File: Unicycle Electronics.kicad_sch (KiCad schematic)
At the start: 0 parts

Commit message: Initial mock
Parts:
- added D1, D?: BXRE-30G20F0-C-83, symbol Device:LED
- added D2: Rear_LED_12V, symbol Device:LED
- added U1: LDH-65-700, symbol LED_Driver:LDH-65-700
- added U?: Stepdown_12V, symbol Converter_DCDC:DC_DC_Buck
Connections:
- new net: D2.2 (K), U1.1 (Vin+), U?.3 (Vout+)
- new net: D1.2 (K), D?.1 (A)
- new net: D?.2 (K), U1.3 (Vout+)
- new net: D1.1 (A), U1.4 (Vout-)
- new net DC_Source: D2.1 (A), U1.2 (Vin-), U?.1 (Vin+), U?.2 (Vin-), U?.4 (Vout-)

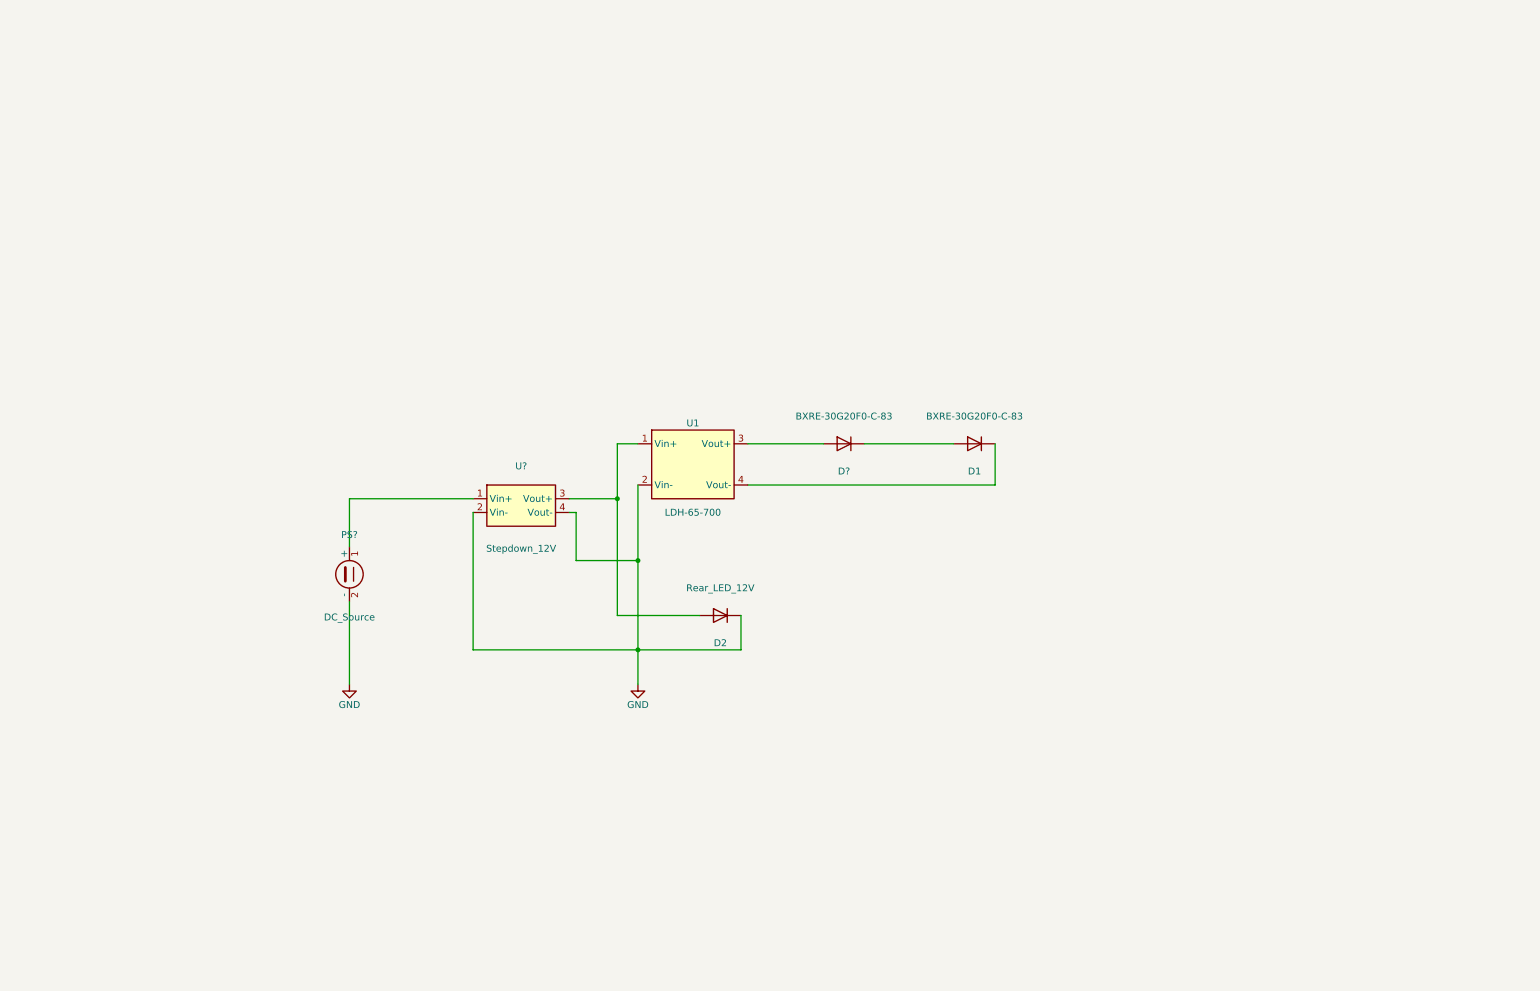
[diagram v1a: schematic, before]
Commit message: Schematic updates
Cleaned it up, added nets

TODO:
Change Diodes to some sort of connector, the LEDs are not on the PCB, they need to be plugged in

3.3v regulator for ESP32

BOOT and EN buttons for ESP32

Add PWM Dimming pins to LED driver

Switch 12v regulator to input on the PCB, meaning use a connector instead of the actual regulator. The regulator does not sit on the PCB
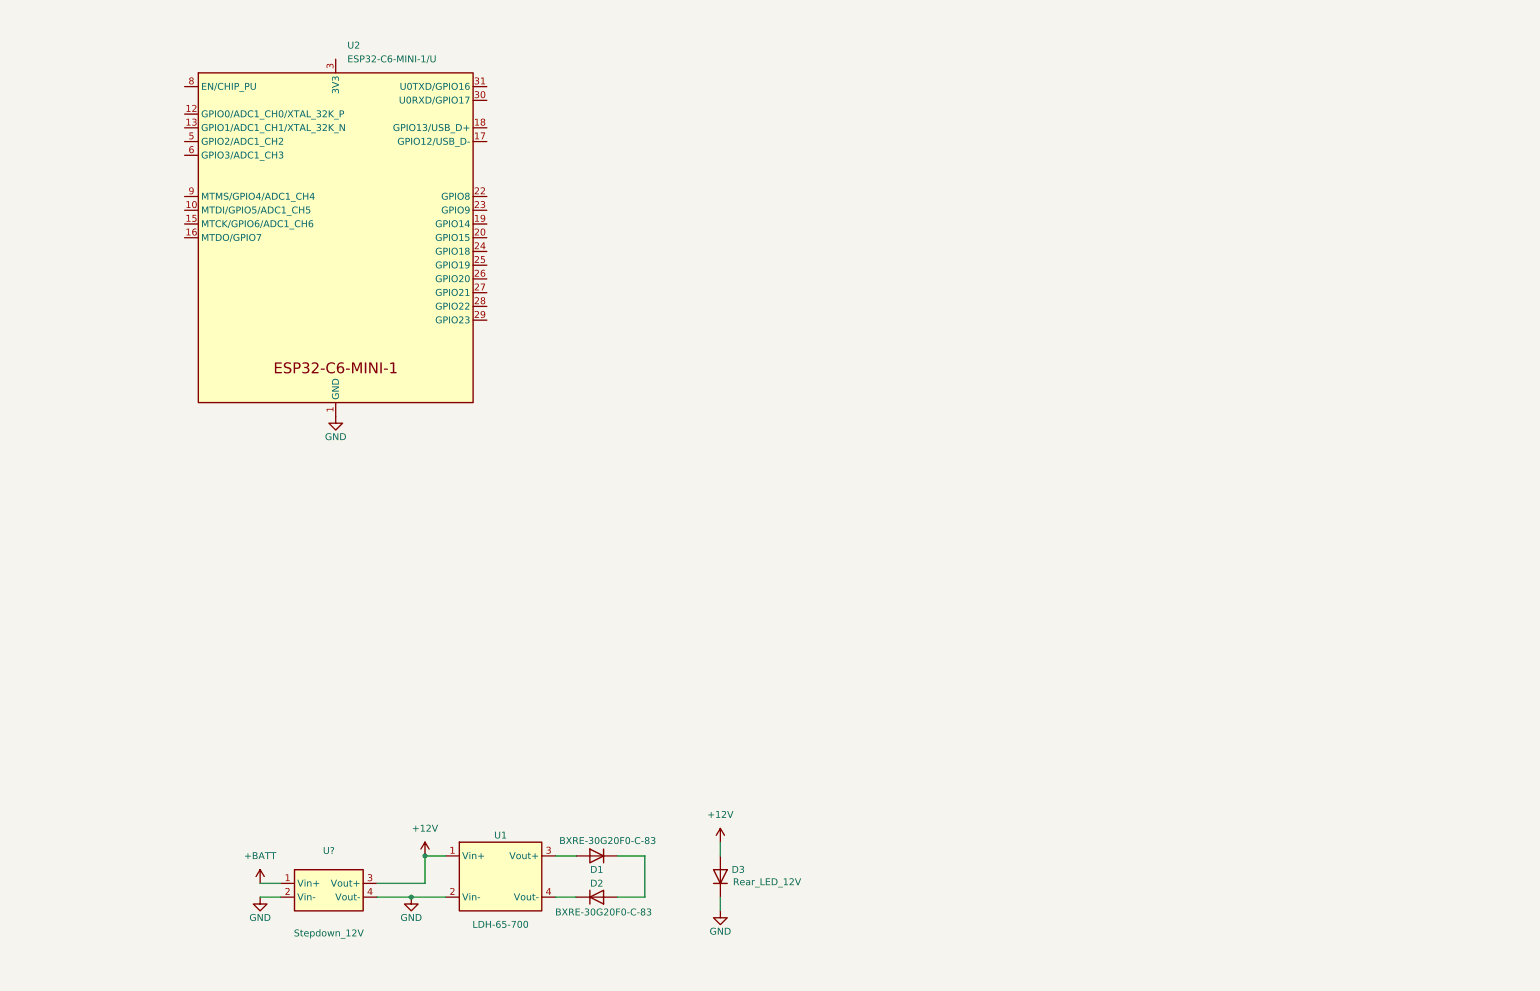
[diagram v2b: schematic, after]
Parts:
- added U2: ESP32-C6-MINI-1/U, PCM_Espressif:ESP32-C6-MINI-1, symbol PCM_Espressif:ESP32-C6-MINI-1/U
- gave numbers to parts that had none: 1
- renumbered D2 to D3
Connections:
- net +12V: now reaches D3.2 (K), U1.1 (Vin+), U?.3 (Vout+)
- net DC_Source renamed GND
- net GND: now also U2.1 (GND), U2.11 (GND), U2.14 (GND), U2.2 (GND), U2.36 (GND), U2.37 (GND), U2.38 (GND), U2.39 (GND), U2.40 (GND), U2.41 (GND), U2.42 (GND), U2.43 (GND), U2.44 (GND), U2.45 (GND), U2.46 (GND), U2.47 (GND), U2.48 (GND), U2.49 (GND), U2.50 (GND), U2.51 (GND), U2.52 (GND), U2.53 (GND); no longer U?.1 (Vin+)
- new net +BATT: U?.1 (Vin+)
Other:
- moved on the sheet: D1, D2, D3, U1, U?

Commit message: schematic update
This is what I have so far—let me know if you need any changes or want me to add anything.
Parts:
- added C1: 10uF, symbol Device:C
- added C2: 22uF, symbol Device:C
- added C3: 100nF, symbol Device:C
- added Q1: 2N7002, Package_TO_SOT_SMD:SOT-23, symbol Transistor_FET:2N7002
- added R1, R2, R4: 10k, symbol Device:R
- added R3: 1k, symbol Device:R
- added SW1: BOOT, symbol Switch:SW_Push
- added SW2: EN/Reset, symbol Switch:SW_Push
- added U3: AMS1117-3.3, Package_TO_SOT_SMD:SOT-223-3_TabPin2, symbol Regulator_Linear:AMS1117-3.3
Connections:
- net +12V: now also C1.1, U3.3 (VI)
- net GND: now also C1.2, C2.2, Q1.1 (S), R4.2, SW1.2, SW2.2, U3.1 (GND)
- net at U2.23 (GPIO9): now also R2.2, SW1.1
- net at U2.8 (EN/CHIP_PU): now also C3.1, R1.2
- new net: C3.2, SW2.1
- new net: Q1.2 (G), R3.2, R4.1
- new net +3.3V: C2.1, R1.1, R2.1, U3.2 (VO)
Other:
- note added: "3.3V Voltage Regulator"
- note added: "BOOT Button (GPIO9)"
- note added: "EN/Reset Button"
- note added: "PWM Dimming Control (GPIO2)"
- moved on the sheet: U2

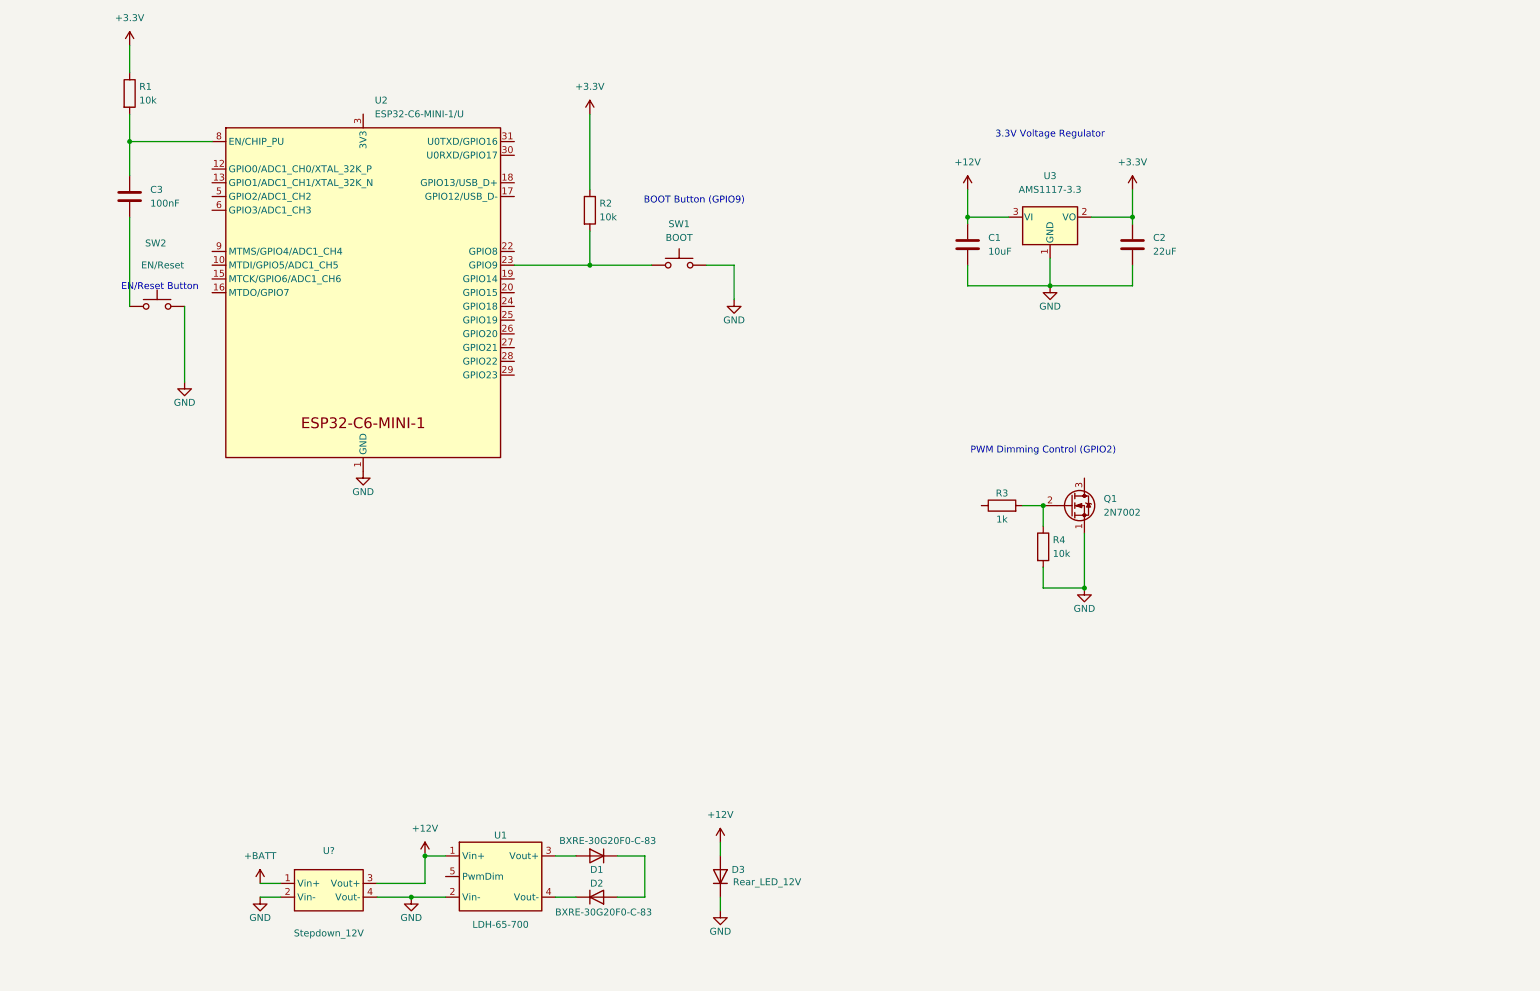
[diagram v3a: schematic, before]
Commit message: Updated TODO list, Changed EN button
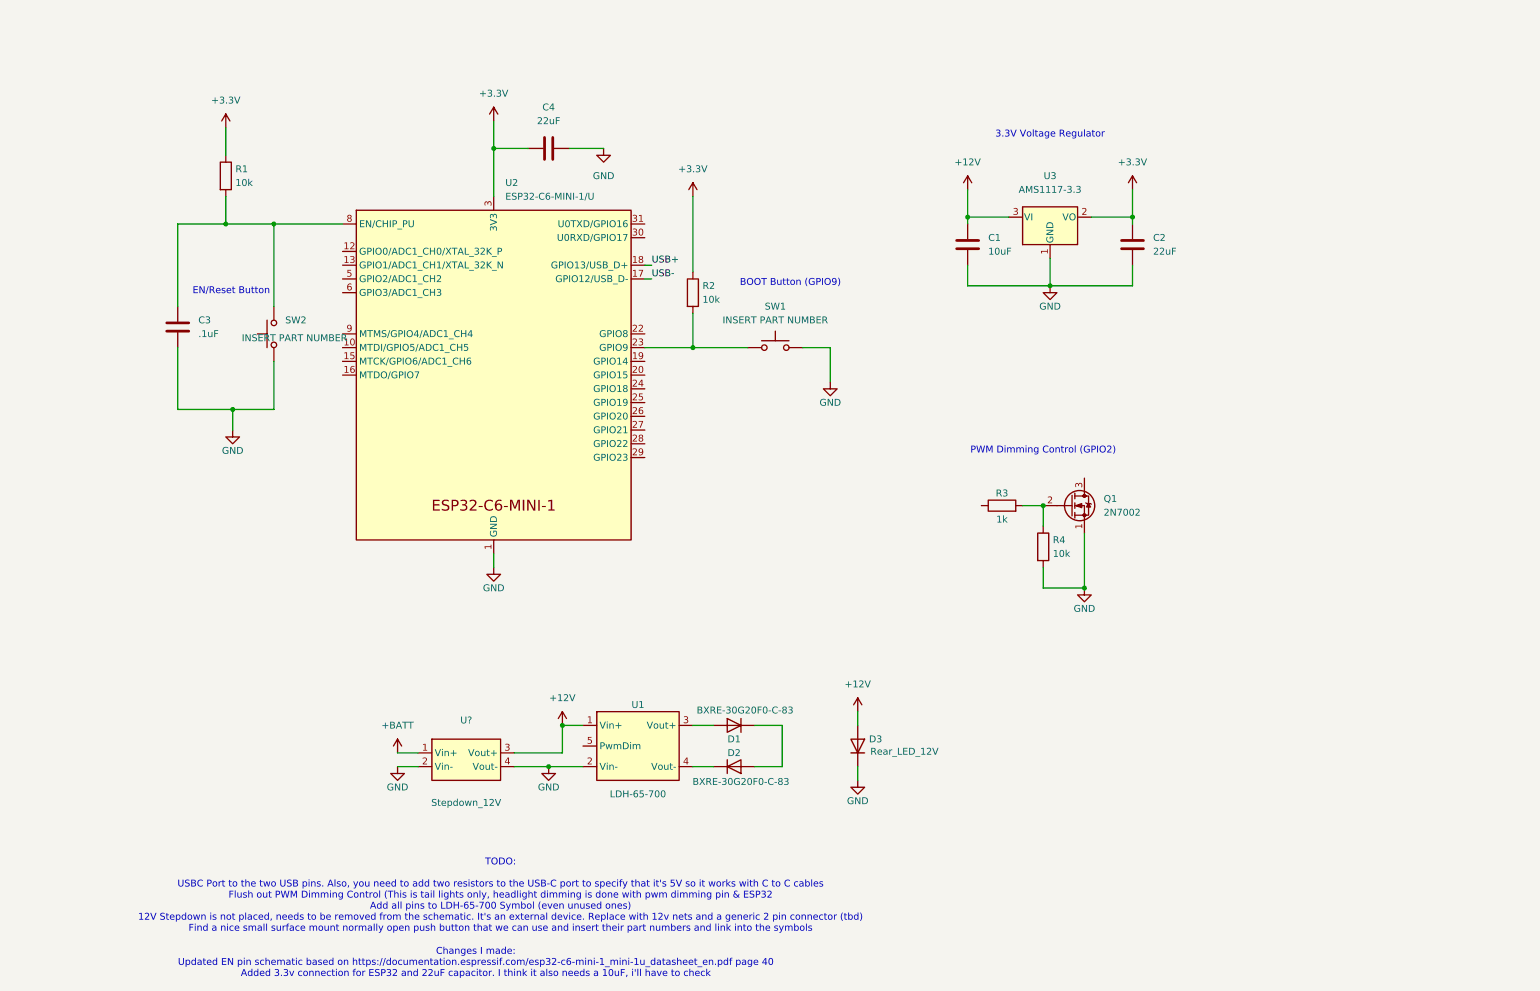
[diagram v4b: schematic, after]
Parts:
- added C4: 22uF, symbol Device:C
- C3: value 100nF -> .1uF
- SW1: value BOOT -> INSERT PART NUMBER
- SW2: value EN/Reset -> INSERT PART NUMBER
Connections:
- net +3.3V: now also U2.3 (3V3), C4.1
- net GND: now also C3.2, SW2.1, C4.2; no longer SW2.2
- net at C3.1, R1.2, U2.8 (EN/CHIP_PU): now also SW2.2
- net USB-: now reaches U2.17 (GPIO12/USB_D-)
- net USB+: now reaches U2.18 (GPIO13/USB_D+)
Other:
- note added: "Changes I made: Updated EN pin schematic based on https://documentation.espressif.com/esp32-c6-mini-1_mini-1u_datasheet_en.pdf page 40 Added 3.3v connection for ESP32 and 22uF capacitor. I think it also needs a 10uF, i'll have to check"
- note added: "TODO: USBC Port to the two USB pins. Also, you need to add two resistors to the USB-C port to specify that it's 5V so it works with C to C cables Flush out PWM Dimming Control (This is tail lights only, headlight dimming is done with pwm dimming pin & ESP32 Add all pins to LDH-65-700 Symbol (even unused ones) 12V Stepdown is not placed, needs to be removed from the schematic. It's an external dev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"
- moved on the sheet: C3, D1, D2, D3, R1, R2, SW1, SW2, U1, U2, U?

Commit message: Schematic Update
Worked on some TODO List
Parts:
- removed R4: 10k, symbol Device:R
- added J1: USB_C, symbol Connector:USB_C_Receptacle_USB2.0
- added R4 (x2): 5.1k, symbol Device:R
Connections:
- net GND: now also U1.4 (Dim+), J1.A1 (GND), J1.A12 (GND), J1.B1 (GND), J1.B12 (GND), J1.S1 (SHIELD), R4.2, R4.2; no longer D3.1 (A)
- net USB+: now also J1.A6 (D+), J1.B6 (D+)
- net USB-: now also J1.A7 (D-), J1.B7 (D-)
- net at Q1.3 (D): now also D3.1 (A)
- net at D2.2 (K): now also U1.5 (Vout+); no longer U1.3 (Vout+)
- net at R3.1: now also U2.5 (GPIO2/ADC1_CH2)
- net at D1.1 (A): now also U1.6 (Vout-); no longer U1.4 (Vout-)
- net at U2.9 (MTMS/GPIO4/ADC1_CH4): now also U1.3 (Dim-)
- new net: J1.A5 (CC1), R4.1
- new net: J1.B5 (CC2), R4.1
- new net +5V: J1.A4 (VBUS), J1.A9 (VBUS), J1.B4 (VBUS), J1.B9 (VBUS)
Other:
- note added: "5.1k CC resistors for USB-C to USB-C cable support"
- note added: "USB-C Port for Programming/Power"
- moved on the sheet: C1, C2, D3, Q1, R3
